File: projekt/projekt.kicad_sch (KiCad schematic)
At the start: 53 parts, among them J1 Conn_01x05, J2 Conn_01x03, J4 87583-0010RHLF, J5 10118192-0001LF, U1 MAX17048G_T10, U2 TPS61022RWUT, U3 MCP73871-2CCI_ML

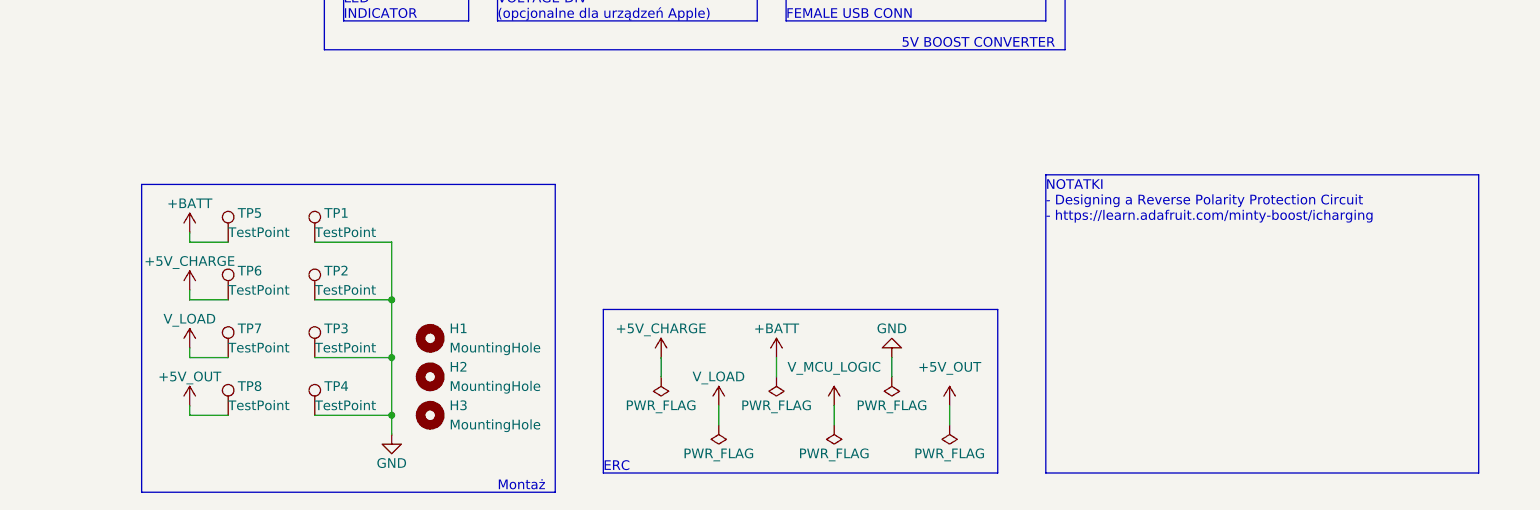
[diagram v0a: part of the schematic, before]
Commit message: MAIN: wersja 2: Poprawiłem termistor, readme update.
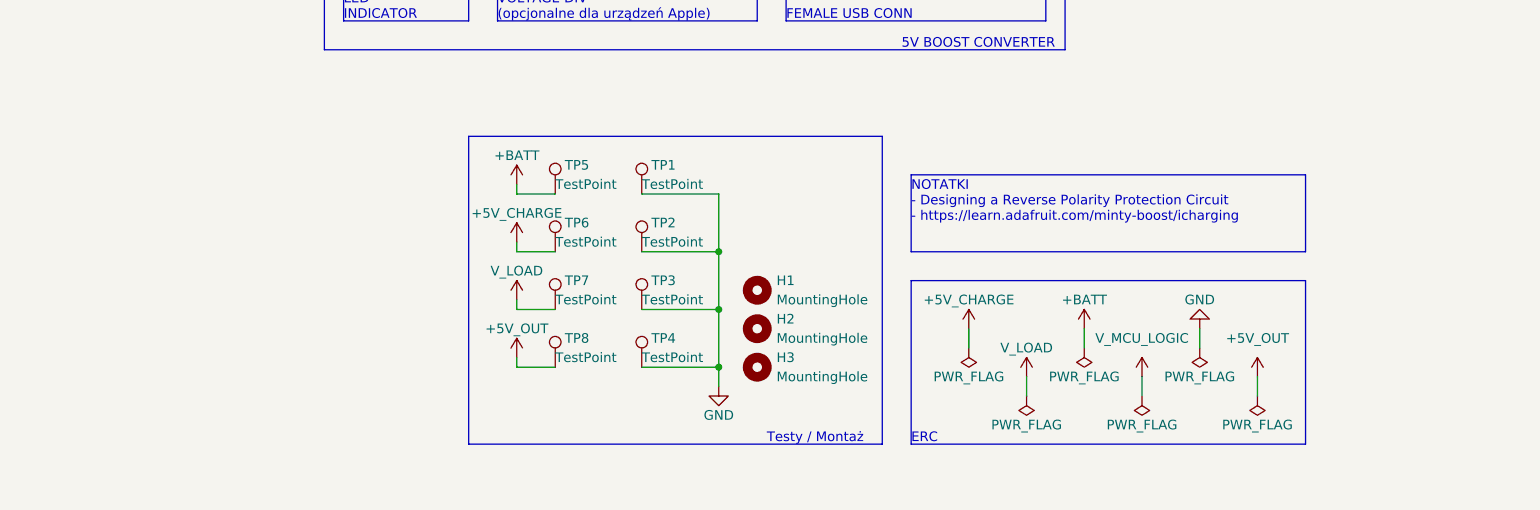
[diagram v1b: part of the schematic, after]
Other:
- note added: "Testy / Montaż"
- note removed: "Montaż"
- moved on the sheet: H1, H2, H3, TP1, TP2, TP3, TP4, TP5, TP6, TP7, TP8

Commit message: MAIN: wersja 2: koniec, wysłane do produkcji.
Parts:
- removed C2: 0.1u, Capacitor_SMD:C_0603_1608Metric, symbol Device:C
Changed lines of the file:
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@@
   (junction (at 151.13 185.42) (diameter 0) (color 0 0 0 0)
   )
+  (junction (at 100.33 73.66) (diameter 0) (color 0 0 0 0)
+  )
   (junction (at 261.62 105.41) (diameter 0) (color 0 0 0 0)
   )
@@
   (junction (at 104.14 152.4) (diameter 0) (color 0 0 0 0)
   )
-  (junction (at 111.76 73.66) (diameter 0) (color 0 0 0 0)
-  )
   (junction (at 48.26 146.05) (diameter 0) (color 0 0 0 0)
   )
@@
     (stroke (width 0) (type default))
   )
-  (wire (pts (xy 111.76 82.55) (xy 111.76 86.36))
-    (stroke (width 0) (type default))
-  )
   (wire (pts (xy 278.13 157.48) (xy 278.13 158.75))
     (stroke (width 0) (type default))
@@
     (stroke (width 0) (type default))
   )
-  (wire (pts (xy 100.33 71.12) (xy 100.33 74.93))
+  (wire (pts (xy 100.33 71.12) (xy 100.33 73.66))
     (stroke (width 0) (type default))
   )
@@
     (stroke (width 0) (type default))
   )
-  (wire (pts (xy 104.14 147.32) (xy 104.14 144.78))
+  (wire (pts (xy 82.55 73.66) (xy 100.33 73.66))
     (stroke (width 0) (type default))
   )
-  (wire (pts (xy 48.26 140.97) (xy 48.26 138.43))
+  (wire (pts (xy 104.14 147.32) (xy 104.14 144.78))
     (stroke (width 0) (type default))
   )
-  (wire (pts (xy 82.55 73.66) (xy 111.76 73.66))
+  (wire (pts (xy 48.26 140.97) (xy 48.26 138.43))
     (stroke (width 0) (type default))
   )
@@
     (stroke (width 0) (type default))
   )
+  (wire (pts (xy 100.33 73.66) (xy 100.33 74.93))
+    (stroke (width 0) (type default))
+  )
   (wire (pts (xy 254 104.14) (xy 254 105.41))
     (stroke (width 0) (type default))
@@
     (stroke (width 0) (type default))
   )
-  (wire (pts (xy 111.76 73.66) (xy 111.76 74.93))
-    (stroke (width 0) (type default))
-  )
   (wire (pts (xy 326.39 107.95) (xy 336.55 107.95))
     (stroke (width 0) (type default))
@@
     (stroke (width 0) (type default))
   )
-  (wire (pts (xy 111.76 67.31) (xy 111.76 73.66))
-    (stroke (width 0) (type default))
-  )
   (wire (pts (xy 256.54 176.53) (xy 256.54 179.07))
     (stroke (width 0) (type default))
@@
     )
   )
-  (symbol (lib_id "power:GND") (at 111.76 86.36 0) (unit 1)
-    (in_bom yes) (on_board yes) (dnp no) (fields_autoplaced)
-    (property "Reference" "#PWR012" (at 111.76 92.71 0)
-      (effects (font (size 1.27 1.27)) hide)
-    )
-    (property "Value" "GND" (at 111.76 91.44 0)
-      (effects (font (size 1.27 1.27)))
-    )
-    (property "Footprint" "" (at 111.76 86.36 0)
-      (effects (font (size 1.27 1.27)) hide)
-    )
-    (property "Datasheet" "" (at 111.76 86.36 0)
-      (effects (font (size 1.27 1.27)) hide)
-    )
-    (pin "1")
-    (instances
-      (project "projekt"
-        (path "/24862f56-230c-4ec9-b409-1e126beaf2a1"
-          (reference "#PWR012") (unit 1)
-        )
-      )
-    )
-  )
   (symbol (lib_id "Device:R") (at 109.22 167.64 0) (unit 1)
     (in_bom yes) (on_board yes) (dnp no)
@@
     )
   )
-  (symbol (lib_id "Device:C") (at 111.76 78.74 0) (unit 1)
-    (in_bom yes) (on_board yes) (dnp no)
-    (property "Reference" "C2" (at 115.57 77.47 0)
-      (effects (font (size 1.27 1.27)) (justify left))
-    )
-    (property "Value" "0.1u" (at 115.57 80.01 0)
-      (effects (font (size 1.27 1.27)) (justify left))
-    )
-    (property "Footprint" "Capacitor_SMD:C_0603_1608Metric" (at 112.7252 82.55 0)
-      (effects (font (size 1.27 1.27)) hide)
-    )
-    (property "Datasheet" "~" (at 111.76 78.74 0)
-      (effects (font (size 1.27 1.27)) hide)
-    )
-    (pin "2")
-    (pin "1")
-    (instances
-      (project "projekt"
-        (path "/24862f56-230c-4ec9-b409-1e126beaf2a1"
-          (reference "C2") (unit 1)
-        )
-      )
-    )
-  )
   (symbol (lib_id "power:GND") (at 87.63 198.12 0) (unit 1)
     (in_bom yes) (on_board yes) (dnp no) (fields_autoplaced)
@@
         )
       )
-    )
-  )
-  (symbol (lib_id "power:+BATT") (at 111.76 67.31 0) (unit 1)
-    (in_bom yes) (on_board yes) (dnp no) (fields_autoplaced)
-    (property "Reference" "#PWR02" (at 111.76 71.12 0)
-      (effects (font (size 1.27 1.27)) hide)
-    )
-    (property "Value" "+BATT" (at 111.76 62.23 0)
-      (effects (font (size 1.27 1.27)))
-    )
-    (property "Footprint" "" (at 111.76 67.31 0)
-      (effects (font (size 1.27 1.27)) hide)
-    )
-    (property "Datasheet" "" (at 111.76 67.31 0)
-      (effects (font (size 1.27 1.27)) hide)
-    )
-    (pin "1")
-    (instances
-      (project "projekt"
-        (path "/24862f56-230c-4ec9-b409-1e126beaf2a1"
-          (reference "#PWR02") (unit 1)
-        )
-      )

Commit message: poprawki
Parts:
- D2: value LED Y -> LED G
- D3: value LED Y -> LED R
- R11, R13: value R -> 51k
- R12: value R -> 43k
- R8: value R -> 75k
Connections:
- net STAT2 renamed CC
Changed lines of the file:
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@@
     (effects (font (size 1.27 1.27)) (justify left bottom))
   )
-  (label "STAT2" (at 60.96 201.93 0) (fields_autoplaced)
+  (label "CC" (at 60.96 201.93 0) (fields_autoplaced)
     (effects (font (size 1.27 1.27)) (justify left bottom))
   )
@@
     (effects (font (size 1.27 1.27)) (justify left bottom))
   )
-  (label "STAT2" (at 151.13 149.86 0) (fields_autoplaced)
+  (label "CC" (at 151.13 149.86 0) (fields_autoplaced)
     (effects (font (size 1.27 1.27)) (justify left bottom))
   )
@@
       (effects (font (size 1.27 1.27)) (justify left))
     )
-    (property "Value" "R" (at 293.37 173.99 0)
+    (property "Value" "51k" (at 293.37 173.99 0)
       (effects (font (size 1.27 1.27)) (justify left))
     )
@@
       (effects (font (size 1.27 1.27)) (justify left))
     )
-    (property "Value" "R" (at 279.4 173.99 0)
+    (property "Value" "51k" (at 279.4 173.99 0)
       (effects (font (size 1.27 1.27)) (justify left))
     )
@@
       (effects (font (size 1.27 1.27)) (justify right))
     )
-    (property "Value" "LED Y" (at 53.34 196.85 90)
+    (property "Value" "LED R" (at 53.34 196.85 90)
       (effects (font (size 1.27 1.27)) (justify right))
     )
@@
       (effects (font (size 1.27 1.27)) (justify left))
     )
-    (property "Value" "R" (at 279.4 163.83 0)
+    (property "Value" "75k" (at 279.4 163.83 0)
       (effects (font (size 1.27 1.27)) (justify left))
     )
@@
       (effects (font (size 1.27 1.27)) (justify left))
     )
-    (property "Value" "R" (at 293.37 163.83 0)
+    (property "Value" "43k" (at 293.37 163.83 0)
       (effects (font (size 1.27 1.27)) (justify left))
     )
@@
       (effects (font (size 1.27 1.27)) (justify right))
     )
-    (property "Value" "LED Y" (at 63.5 196.85 90)
+    (property "Value" "LED G" (at 63.5 196.85 90)
       (effects (font (size 1.27 1.27)) (justify right))
     )
